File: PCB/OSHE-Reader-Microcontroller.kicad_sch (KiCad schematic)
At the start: 5 parts

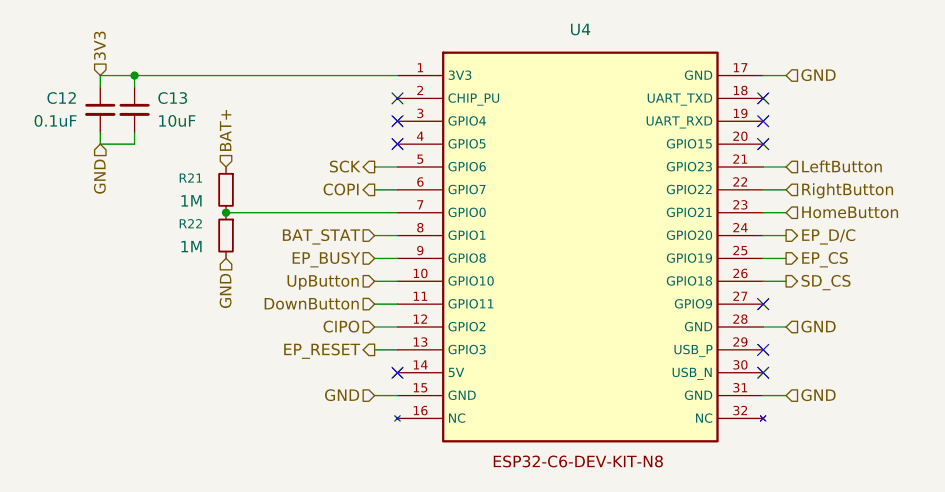
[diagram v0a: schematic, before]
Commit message: More work done on PCB. TODO: Battery Charging and Buck Converter
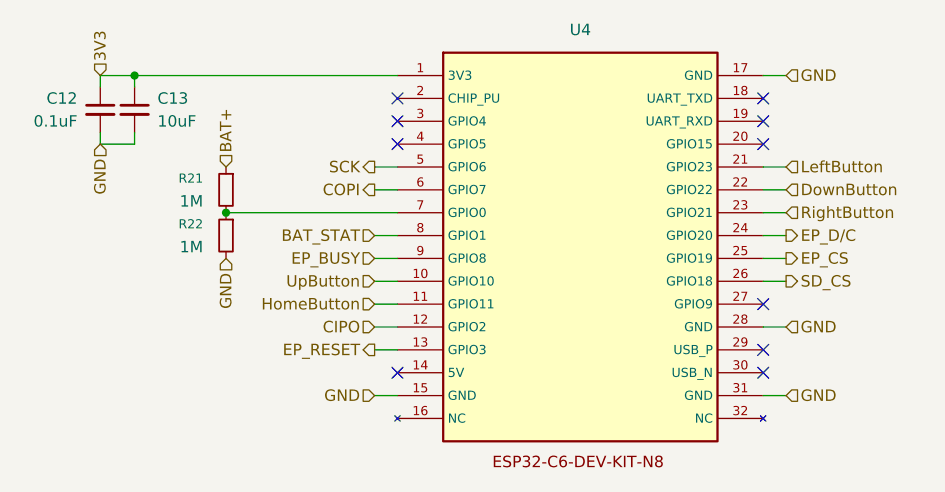
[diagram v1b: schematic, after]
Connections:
- net DownButton: now also U4.22 (GPIO22); no longer U4.11 (GPIO11)
- net HomeButton: now also U4.11 (GPIO11); no longer U4.23 (GPIO21)
- net RightButton: now also U4.23 (GPIO21); no longer U4.22 (GPIO22)
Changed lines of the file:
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@@
-		)
-	)
-	(hierarchical_label "DownButton"
-		(shape input)
-		(at 60.96 74.93 180)
-		(effects
-			(font
-				(size 1.27 1.27)
-			)
-			(justify right)
 		)
 	)
@@
 		)
 	)
+	(hierarchical_label "DownButton"
+		(shape input)
+		(at 106.68 62.23 0)
+		(effects
+			(font
+				(size 1.27 1.27)
+			)
+			(justify left)
+		)
+	)
 	(hierarchical_label "UpButton"
 		(shape input)
@@
 		)
 	)
-	(hierarchical_label "RightButton"
-		(shape input)
-		(at 106.68 62.23 0)
-		(effects
-			(font
-				(size 1.27 1.27)
-			)
-			(justify left)
-		)
-	)
 	(hierarchical_label "LeftButton"
 		(shape input)
@@
 	(hierarchical_label "HomeButton"
 		(shape input)
+		(at 60.96 74.93 180)
+		(effects
+			(font
+				(size 1.27 1.27)
+			)
+			(justify right)
+		)
+	)
+	(hierarchical_label "RightButton"
+		(shape input)
 		(at 106.68 64.77 0)
